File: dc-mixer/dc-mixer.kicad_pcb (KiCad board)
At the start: 2 copper layers, 50.8 x 25.4 mm, 22 parts, among them J1 Conn_01x01_Female, J2 Conn_01x01_Female, J3 Conn_01x01_Female, J4 Conn_01x01_Female, J5 Conn_01x01_Female, J6 Conn_01x01_Female, J7 Conn_01x01_Female, J8 Conn_01x04_Male, J9 Conn_01x01_Female, U1 TL072

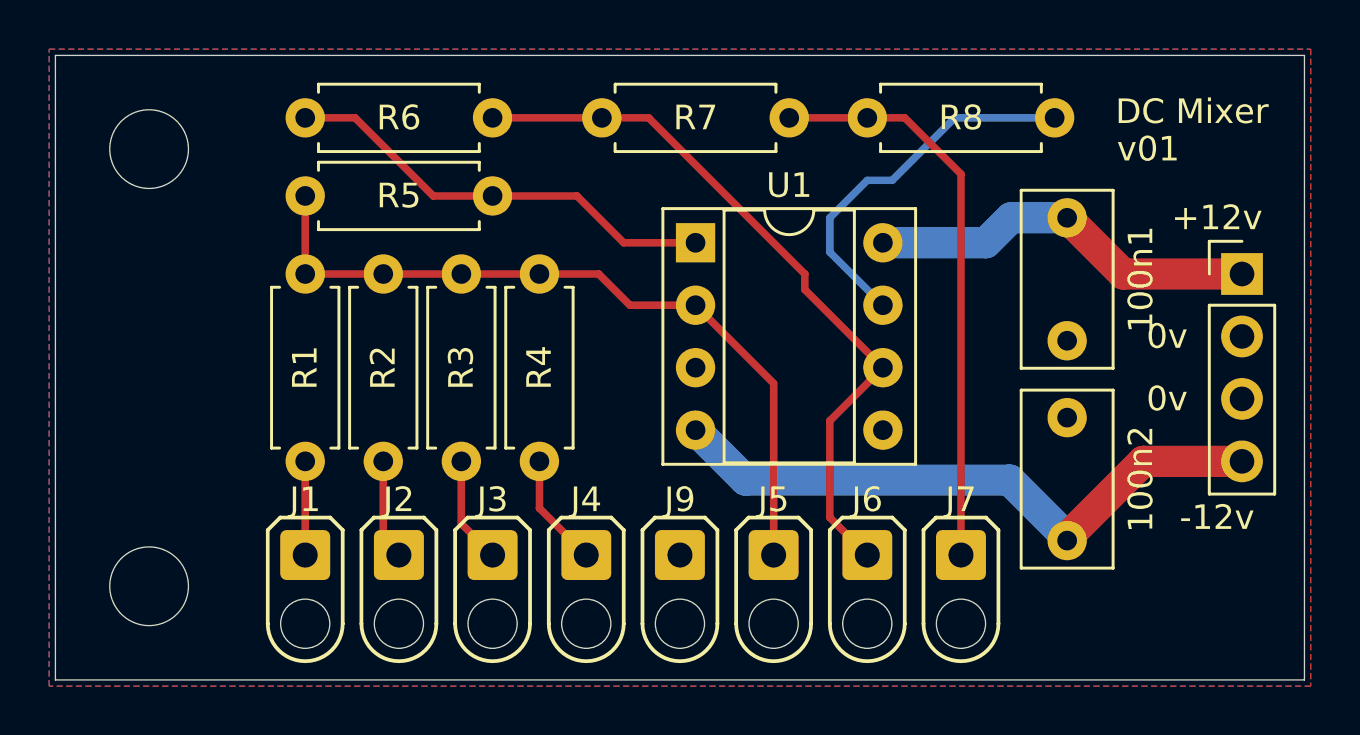
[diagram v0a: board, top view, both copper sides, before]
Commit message: adding opamp feedback caps to dc mixer
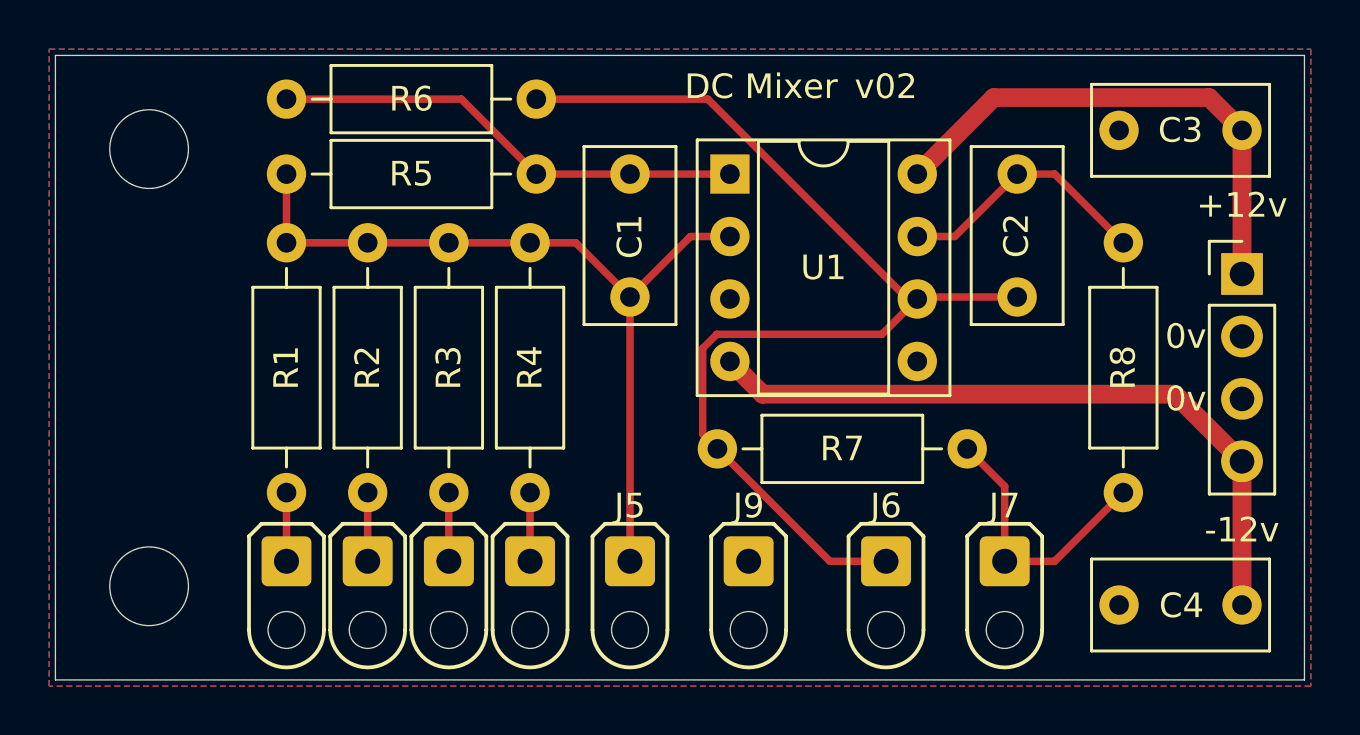
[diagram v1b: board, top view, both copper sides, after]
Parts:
- removed 100n1, 100n2: C, Capacitor_THT:C_Rect_L7.0mm_W3.5mm_P5.00mm
- removed REF** (x2): MountingHole_3.2mm_M3, MountingHole:MountingHole_3.2mm_M3
- added C1: 47pF, Capacitor_THT:C_Rect_L7.0mm_W3.5mm_P5.00mm, F.Cu at (125.0, 106.4)
- added C2: 47pF, Capacitor_THT:C_Rect_L7.0mm_W3.5mm_P5.00mm, F.Cu at (140.7, 106.4)
- added C3: 100nF, Capacitor_THT:C_Rect_L7.0mm_W3.5mm_P5.00mm, F.Cu at (149.9, 104.6)
- added C4: 100nF, Capacitor_THT:C_Rect_L7.0mm_W3.5mm_P5.00mm, F.Cu at (144.9, 124.0)
- added H1: MountingScrew_M3_Flathead, MountingHole:MountingHole_3.2mm_M3, F.Cu at (105.4, 123.2)
- added H2: MountingScrew_M3_Flathead, MountingHole:MountingHole_3.2mm_M3, F.Cu at (105.4, 105.4)
- R1, R2, R3, R4, R5, R6, R7, R8: footprint Resistor_THT:R_Axial_DIN0207_L6.3mm_D2.5mm_P7.62mm_Horizontal -> Resistor_THT:R_Axial_DIN0207_L6.3mm_D2.5mm_P10.16mm_Horizontal
- moved R8 18.5 mm to (145.0, 119.4), turned to 90 degrees
- moved R7 15.3 mm to (138.7, 117.6)
- moved J5 5.85 mm to (125.0, 122.2)
- moved U1 3.12 mm to (129.0, 106.4)
- moved J9 2.81 mm to (129.8, 122.2)
- moved J4 2.30 mm to (120.9, 122.2)
- moved R5 1.99 mm to (121.2, 106.4)
- moved R6 1.93 mm to (121.2, 103.4)
- moved J3 1.80 mm to (117.6, 122.2)
- moved J7 1.80 mm to (140.2, 122.2)
- moved R1 1.48 mm to (111.0, 109.2)
- moved R2 1.42 mm to (114.3, 109.2)
- moved R3 1.37 mm to (117.6, 109.2)
- moved R4 1.33 mm to (120.9, 109.2)
- moved J2 1.30 mm to (114.3, 122.2)
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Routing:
- net Net-(C2-Pad2): track 29.6 -> 45.6 mm
- net Net-(J7-Pad1): track 23.4 -> 11.2 mm
- net +12V: track 15.5 -> 20.9 mm
- net Net-(C2-Pad1): track 15.3 -> 10.6 mm
- net -12V: track 24.8 -> 28.4 mm
- net Net-(C1-Pad2): track 31.1 -> 33.5 mm
- net Net-(J4-Pad1): track 4.60 -> 2.79 mm
- net Net-(J3-Pad1): track 4.34 -> 2.79 mm
- net Net-(C1-Pad1): track 18.0 -> 19.3 mm
- net Net-(J2-Pad1): track 4.07 -> 2.79 mm
- net Net-(J1-Pad1): track 3.81 -> 2.79 mm
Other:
- board text added: "v02"
- board text removed: "v01"
